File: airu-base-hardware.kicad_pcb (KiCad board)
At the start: 2 copper layers, 63.5 x 107.6 mm, 181 parts, among them IC1 ADS7828E/2K5, IC2 ADS7828E/2K5, J1 12402012E212A, J10 NPPN101BFLC-RC, J11 NPPN101BFLC-RC, J12 533980571, J13 533980571, J14 533980571, J15 533980471, J16 U.FL-R-SMT(01), J17 S8411-45R, J18 10129380-902001BLF, J19 533980771, J2 DM3AT-SF-PEJM5, J21 95278-801A10LF, J3 0787881014, J4 0787881014, J5 0877591014, J6 5013310607, J7 532610871, J8 533980271, J9 20021121-00006C4LF, Q1 BSS138G, Q2 BSS138G, Q3 BSS138G, SW1 B3F-3100, U1 ESP32-S3-WROOM-1-N8, U10 AP22811AW5-7, U11 TPS72748DSER, U12 MAX40200AUK, U2 MCP7940NT-I_SN, U3 TPS2054BDR, U4 SN74LV4052ADR, U5 PCAL6524HEAZ, U6 BME280, U7 LC76GABMD, U8 LM66200DRLR, U9 AP22811AW5-7, Y1 32.768K kHz

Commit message: Layout draft
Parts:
- removed PS1: TPS62162DSGR, airu_library:SON50P200X200X80-9N
- removed R25: 1.21M, Resistor_SMD:R_0603_1608Metric
- removed R26: 383K, Resistor_SMD:R_0603_1608Metric
- removed R27: 100K, Resistor_SMD:R_0603_1608Metric
- added C69: 100nF, Capacitor_SMD:C_0603_1608Metric, F.Cu at (134.8, 114.5)
- added C70: 22uF, Capacitor_SMD:C_0603_1608Metric, F.Cu at (130.1, 107.9)
- added G***: LOGO, airu_library:logo, B.Cu at (113.7, 133.4)
- added U13: AP63203WU-7, airu_library:AP63203WU-7_DIO, F.Cu at (135.6, 111.9)
- C16, C17, C49, C62: moved to B.Cu
- C33, C34: value 10pF -> 6pF
- C52: value 68uF -> 100nF; footprint Capacitor_SMD:C_1206_3216Metric -> Capacitor_SMD:C_0603_1608Metric
- L49: value 2.2uH -> 3.9uH; footprint airu_library:IND_VLS3012HBX_TDK -> airu_library:IND_ASPI-0628-3R9M-T1
- R31, R32, U6: moved to F.Cu
- Y1: value 32.768K kHz -> 32.768KHZ
- moved J18 53.0 mm to (152.5, 127.9), turned to 0 degrees
- moved C24 49.2 mm to (148.3, 78.0), turned to 180 degrees
- moved U3 40.6 mm to (145.8, 73.1)
- moved TP11 38.1 mm to (129.4, 88.4)
- moved C57 36.4 mm to (147.4, 81.6), turned to 90 degrees
- moved TP10 35.0 mm to (121.3, 88.8)
- moved U11 32.5 mm to (145.3, 81.5), turned to 0 degrees
- moved R31 29.2 mm to (102.1, 133.8), turned to -90 degrees
- moved C58 28.6 mm to (143.1, 81.5), turned to 90 degrees
- moved TP9 27.8 mm to (100.3, 51.3)
- moved TP15 27.2 mm to (100.4, 57.6)
- moved R32 27.0 mm to (103.7, 133.8), turned to -90 degrees
- moved TP14 25.6 mm to (100.4, 54.5)
- moved C63 23.3 mm to (115.8, 59.0), turned to -90 degrees
- moved C64 22.6 mm to (114.3, 59.0), turned to -90 degrees
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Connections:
- net I2C_SD renamed I2S_SD
- net Net-(D9-K) renamed /Internal Sensor/RF_IN_EXT
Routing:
- net GND: track 0.00 -> 373.1 mm, vias 0 -> 374
- net +5V: track 0.00 -> 209.0 mm, vias 0 -> 5
- net +3V3_IDLE: track 0.00 -> 142.5 mm, vias 0 -> 7
- net +3V3: track 0.00 -> 142.5 mm, vias 0 -> 28
- net +4V8_A: track 0.00 -> 110.4 mm, vias 0 -> 7
- net INT_I2C_SDA: track 0.00 -> 108.8 mm, vias 0 -> 6
- net INT_I2C_SCL: track 0.00 -> 107.1 mm, vias 0 -> 6
- net GNSS_RST: track 0.00 -> 90.6 mm, vias 0 -> 3
- net PM_UART_RX: track 0.00 -> 83.4 mm, vias 0 -> 3
- net +5V_IDLE: track 0.00 -> 74.2 mm, vias 0 -> 2
- net PM_UART_TX: track 0.00 -> 74.2 mm, vias 0 -> 3
- net NET_HWID2: track 0.00 -> 70.4 mm, vias 0 -> 3
- net /MCU/EN: track 0.00 -> 70.2 mm, vias 0 -> 5
- net APP_UART_RX: track 0.00 -> 65.4 mm, vias 0 -> 2
- net +5V_NET_IN: track 0.00 -> 65.1 mm
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- added copper zone on In2.Cu, net +3V3
- added copper zone on B.Cu, net GND
- added copper zone on F.Cu, net GND
- added copper zone on In1.Cu, net GND
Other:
- copper layers 2 -> 4
- board text added: "+3V3"
- board text added: "+5V"
- board text added: "0"
- board text added: "0 mils"
- board text added: "0.02"
- board text added: "0.1500 mm / 0.1500 mm"
- board text added: "0.3000 mm"
- board text added: "0.3937 mils"
- board text added: "0.59843 mils"
- board text added: "1"
- board text added: "1.37795 mils"
- board text added: "1.6062 mm"
- board text added: "1_0"
- board text added: "1_1"
- board text added: "1_2"
- board text added: "1_3"
- board text added: "1_4"
- board text added: "1_5"
- board text added: "1_6"
- board text added: "1_7"
- board text added: "2_0"
- board text added: "2_1"
- board text added: "2_2"
- board text added: "3.3"
- board text added: "3V3"
- board text added: "3V3_GPS"
- board text added: "3V3_IDLE"
- board text added: "3_0"
- board text added: "3_1"
- board text added: "3_2"
- board text added: "4"
- board text added: "4.5"
- board text added: "41.92913 mils"
- board text added: "4V8_A"
- board text added: "4_0"
- board text added: "4_1"
- board text added: "4_2"
- board text added: "5V"
- board text added: "5V_IDLE"
- board text added: "5V_NET_IN"
- board text added: "5V_PROG"
- board text added: "5V_VBUS"
- board text added: "63.5000 mm x 107.6000 mm"
- board text added: "8.28346 mils"
- board text added: "AFE0"
- board text added: "AFE1"
- board text added: "AFE2"
- board text added: "APP_RX"
- board text added: "APP_TX"
- board text added: "AirU Pro Base v1.0.0 11/2025"
- board text added: "B.Cu"
- board text added: "B.Mask"
- board text added: "B.Paste"
- board text added: "B.Silkscreen"
- board text added: "BOARD CHARACTERISTICS"
- board text added: "Board Thickness:"
- board text added: "Board overall dimensions:"
- board text added: "Bottom Silk Screen"
- board text added: "Bottom Solder Mask"
- board text added: "Bottom Solder Paste"
- board text added: "CABLE DIRECTION"
- board text added: "Castellated pads:"
- board text added: "Color"
- board text added: "Copper Finish:"
- board text added: "Copper Layer Count:"
- board text added: "Dielectric 1"
- board text added: "Dielectric 2"
- board text added: "Dielectric 3"
- board text added: "EXT I2C"
- board text added: "EXT UART0"
- board text added: "EXT UART1"
- board text added: "Edge card connectors:"
- board text added: "Epsilon R"
- board text added: "Extra I/O"
- board text added: "F.Cu"
- board text added: "F.Mask"
- board text added: "F.Paste"
- board text added: "F.Silkscreen"
- board text added: "FAN"
- board text added: "FR4"
- board text added: "GND"
- board text added: "GNSS ANTENNA"
- board text added: "GNSS_RX"
- board text added: "GNSS_TX"
- board text added: "I2S_SCK"
- board text added: "I2S_SD"
- board text added: "I2S_WS"
- board text added: "INT_SCL"
- board text added: "INT_SDA"
- board text added: "Impedance Control:"
- board text added: "In1.Cu"
- board text added: "In2.Cu"
- board text added: "Layer Name"
- board text added: "Loss Tangent"
- board text added: "Material"
- board text added: "Min hole diameter:"
- board text added: "Min track/spacing:"
- board text added: "NETWORK CARD"
- board text added: "No"
- board text added: "None"
- board text added: "Not specified"
- board text added: "OPC-N3"
- board text added: "PMS"
- board text added: "PT_0"
- board text added: "PT_1"
- board text added: "PT_2"
- board text added: "PWR"
- board text added: "PWR_EN"
- board text added: "Plated Board Edge:"
- board text added: "SPI"
- board text added: "THERMISTOR"
- board text added: "Thickness (mils)"
- board text added: "Top Silk Screen"
- board text added: "Top Solder Mask"
- board text added: "Top Solder Paste"
- board text added: "Type"
- board text added: "WIFI JPR"
- board text added: "Yes"
- board text added: "copper"
- board text added: "core"
- board text added: "prepreg"

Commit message: Refine layout
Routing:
- net GND: track 373.1 -> 378.0 mm
- net +3V3: track 142.5 -> 144.1 mm, vias 28 -> 29
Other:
- board text added: "11.81 mils"
- board text added: "2500.00 mils x 4236.22 mils"
- board text added: "5.91 mils / 5.91 mils"
- board text added: "63.24 mils"
- board text added: "A0_CH0"
- board text added: "A0_CH1"
- board text added: "A0_CH2"
- board text added: "A0_CH3"
- board text added: "A0_CH4"
- board text added: "A0_CH5"
- board text added: "A0_CH6"
- board text added: "A0_CH7"
- board text added: "A1_CH0"
- board text added: "A1_CH1"
- board text added: "A1_CH2"
- board text added: "A1_CH3"
- board text added: "A1_CH4"
- board text added: "A1_CH5"
- board text added: "A1_CH6"
- board text added: "A1_CH7"
- board text added: "AFE0 PINOUT"
- board text added: "AFE1 PINOUT"
- board text added: "AFE2 PINOUT"
- board text added: "X"
- board text removed: "0.1500 mm / 0.1500 mm"
- board text removed: "0.3000 mm"
- board text removed: "1.6062 mm"
- board text removed: "63.5000 mm x 107.6000 mm"

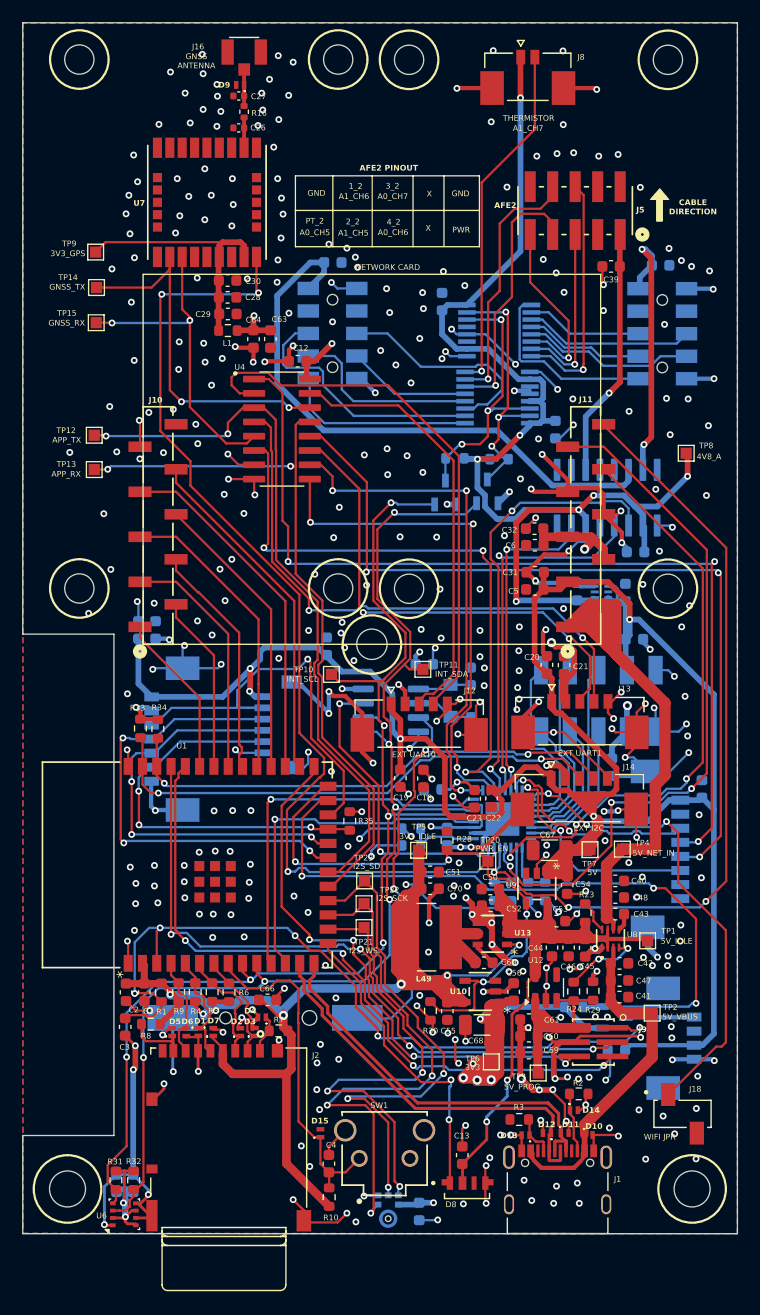
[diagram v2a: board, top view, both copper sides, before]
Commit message: More mfg readiness tweaks; ext power hdr
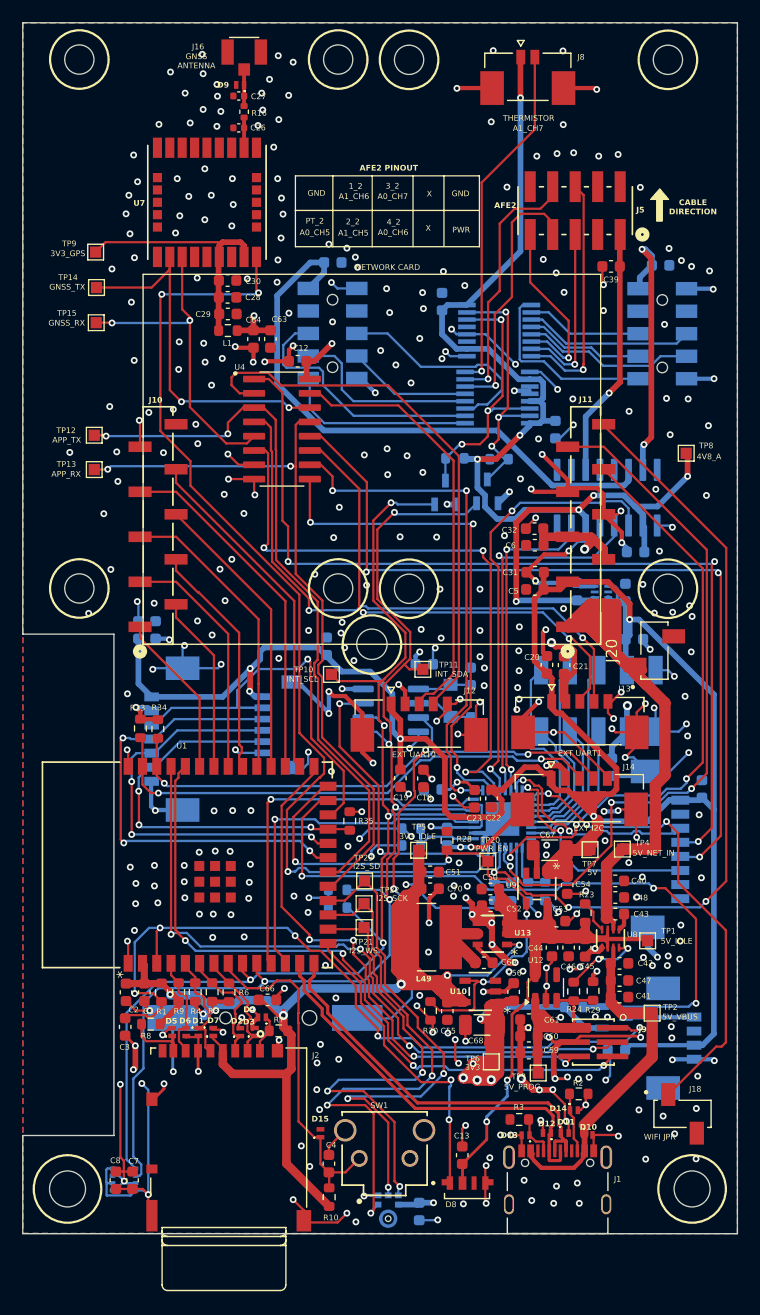
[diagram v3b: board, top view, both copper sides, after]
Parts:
- added J20: 10129380-902001BLF, airu_library:AMPHENOL_10129380-902001BLF, F.Cu at (150.0, 86.7)
- C7, C8: moved to F.Cu
- R31, R32, U6: moved to B.Cu
- moved R32 31.5 mm to (121.8, 108.0), turned to 0 degrees
- moved R31 31.2 mm to (121.8, 109.6), turned to 0 degrees
- moved U6 3.09 mm to (102.8, 133.7)
- moved C7 0.28 mm to (103.6, 133.8), turned to -90 degrees
- moved C8 0.28 mm to (102.1, 133.8), turned to -90 degrees
- moved G*** 0.23 mm to (113.9, 133.5)
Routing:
- net +3V3: track 144.1 -> 137.3 mm, vias 29 -> 30
- net +5V_NET_IN: track 65.1 -> 68.2 mm
- net INT_I2C_SCL: track 107.1 -> 107.7 mm, vias 6 -> 5
- net GND: track 378.0 -> 377.4 mm, vias 374 -> 377
- net INT_I2C_SDA: vias 6 -> 5

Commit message: Tweaks
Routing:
- net GND: track 377.4 -> 379.3 mm, vias 377 -> 376
- net PM_SET: track 19.2 -> 19.7 mm
